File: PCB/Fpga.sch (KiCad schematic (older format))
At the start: 17 parts

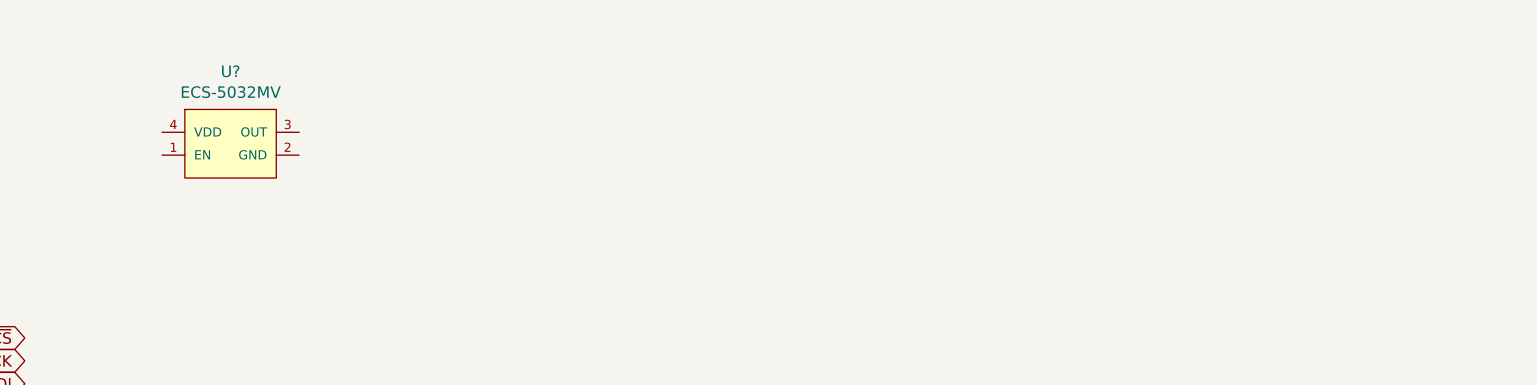
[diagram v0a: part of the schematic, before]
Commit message: Connect oscillator to power
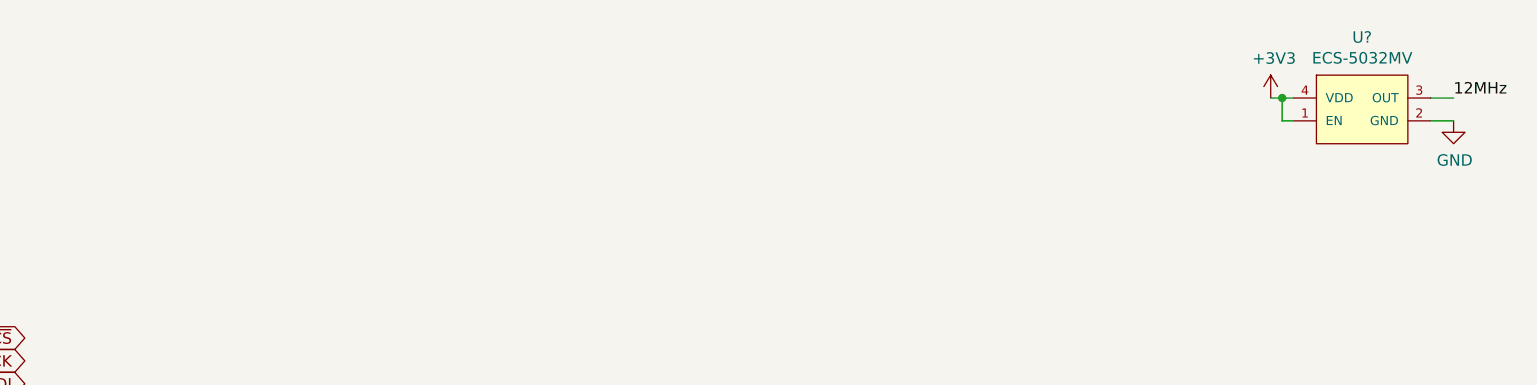
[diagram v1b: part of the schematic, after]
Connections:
- net +3V3: now also U?.1 (EN), U?.4 (VDD)
- net GND: now also U?.2 (GND)
- net 12MHz: now reaches U?.3 (OUT)
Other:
- moved on the sheet: U?
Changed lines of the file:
@@
 L Parts:ECS-5032MV U?
 U 1 1 5DD22CF7
-P 5450 1150
-F 0 "U?" H 5450 1465 50  0000 C CNN
-F 1 "ECS-5032MV" H 5450 1374 50  0000 C CNN
-F 2 "Parts:ECS-5032MV" H 5450 850 50  0001 C CNN
-F 3 "https://ecsxtal.com/ecs-5032mv" H 5450 750 50  0001 C CNN
-	1    5450 1150
+P 10400 1000
+F 0 "U?" H 10400 1315 50  0000 C CNN
+F 1 "ECS-5032MV" H 10400 1224 50  0000 C CNN
+F 2 "Parts:ECS-5032MV" H 10400 700 50  0001 C CNN
+F 3 "https://ecsxtal.com/ecs-5032mv" H 10400 600 50  0001 C CNN
+	1    10400 1000
 	1    0    0    -1
 $EndComp
@@
 Text GLabel 5750 5800 0    50   Input ~ 0
 FPGA-LINK4
+$Comp
+L power:+3V3 #PWR?
+U 1 1 5DD97BF5
+P 10000 950
+F 0 "#PWR?" H 10000 800 50  0001 C CNN
+F 1 "+3V3" H 10015 1123 50  0000 C CNN
+F 2 "" H 10000 950 50  0001 C CNN
+F 3 "" H 10000 950 50  0001 C CNN
+	1    10000 950
+	1    0    0    -1
+$EndComp
+Wire Wire Line
+	10000 950  10050 950
+$Comp
+L power:GND #PWR?
+U 1 1 5DD9CD01
+P 10800 1050
+F 0 "#PWR?" H 10800 800 50  0001 C CNN
+F 1 "GND" H 10805 877 50  0000 C CNN
+F 2 "" H 10800 1050 50  0001 C CNN
+F 3 "" H 10800 1050 50  0001 C CNN
+	1    10800 1050
+	1    0    0    -1
+$EndComp
+Wire Wire Line
+	10700 1050 10800 1050
+Text Label 10800 950  0    50   ~ 0
+12MHz
+Wire Wire Line
+	10700 950  10800 950
+Wire Wire Line
+	10050 950  10050 1050
+Wire Wire Line
+	10050 1050 10100 1050
+Connection ~ 10050 950
+Wire Wire Line
+	10050 950  10100 950
 $EndSCHEMATC

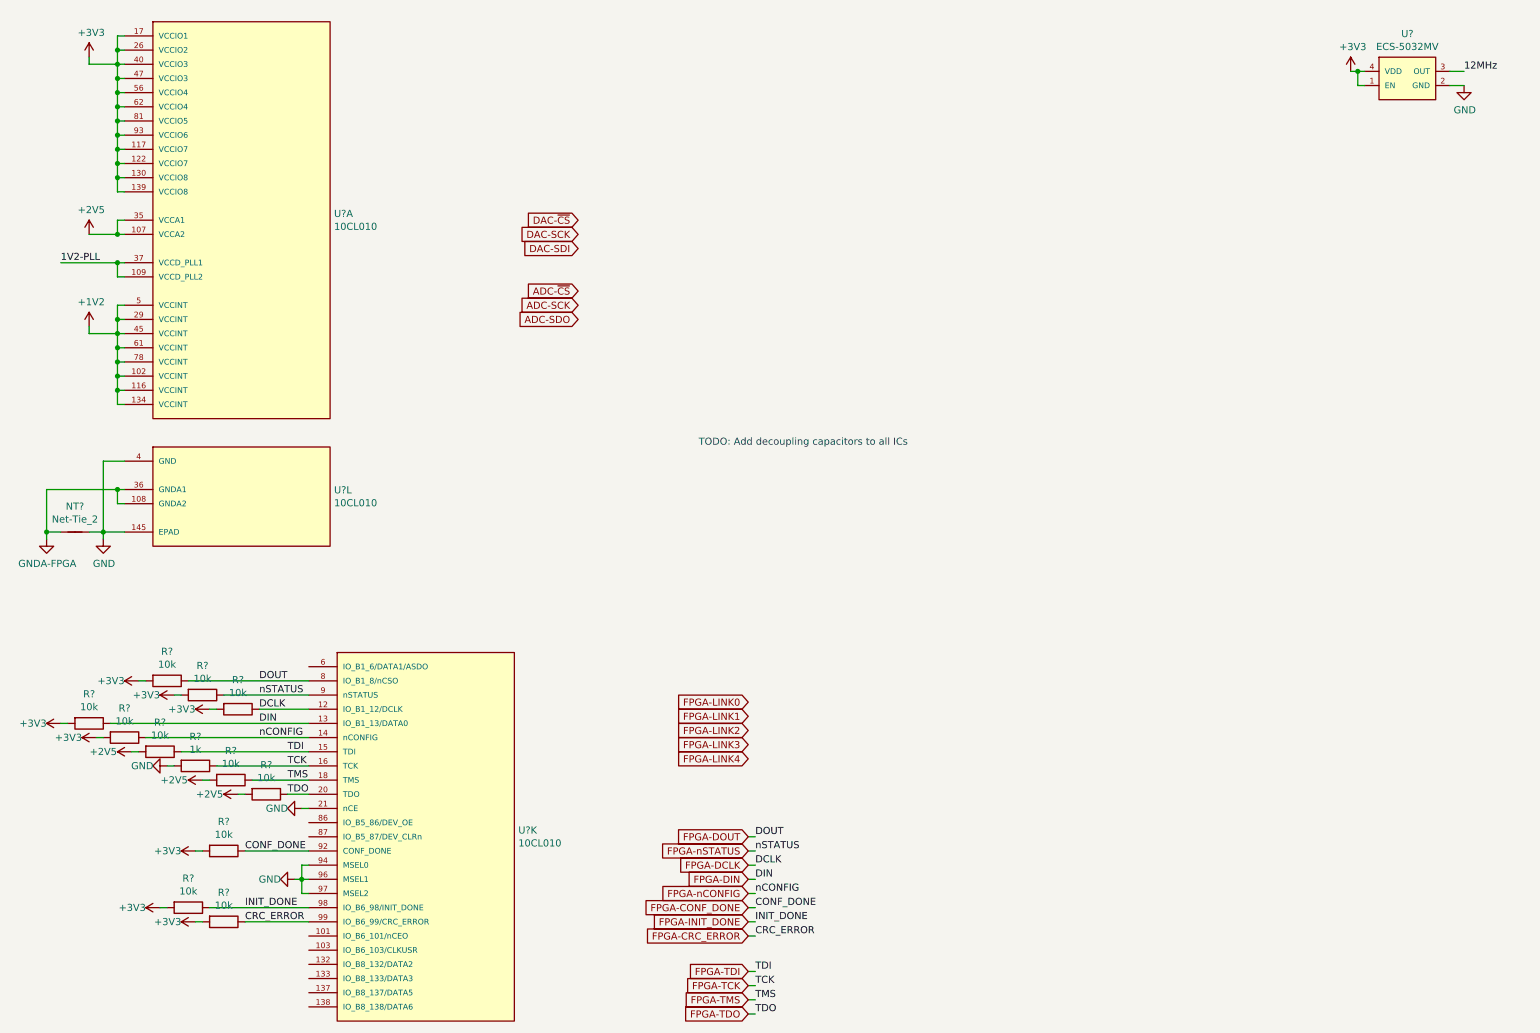
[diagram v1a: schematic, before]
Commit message: Added low-noise supply rails, changed 100nF capacitors to 0603 footprint, fixed ENS210 footprint, added decoupling capacitors to microcontroller
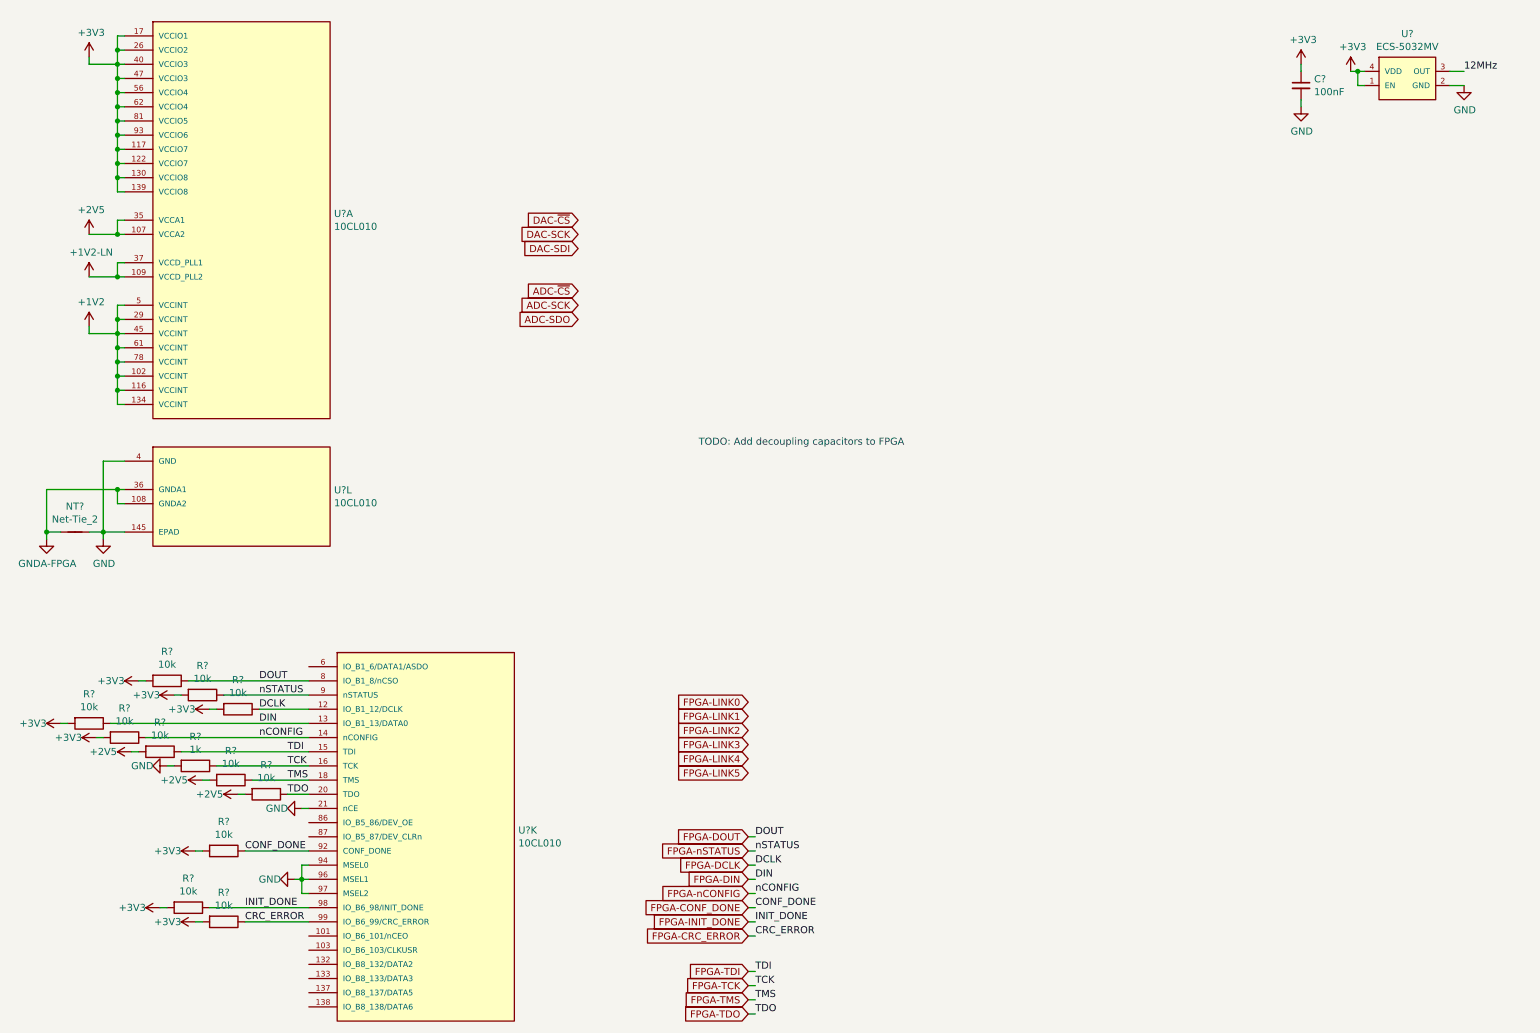
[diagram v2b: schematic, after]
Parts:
- added C?: 100nF, Capacitors_SMD:C_0603_HandSoldering, symbol Device:C_Small
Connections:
- net +3V3: now also C?.1
- net GND: now also C?.2
- net 1V2-PLL renamed +1V2-LN
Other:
- note added: "TODO: Add decoupling capacitors to FPGA"
- note removed: "TODO: Add decoupling capacitors to all ICs"
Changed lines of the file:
@@
 Wire Wire Line
 	1300 2400 1350 2400
-Text Label 900  2300 0    50   ~ 0
-1V2-PLL
 Wire Wire Line
 	1300 2300 1300 2400
-Wire Wire Line
-	900  2300 1300 2300
-Connection ~ 1300 2300
 Text GLabel 4550 2000 0    50   Input ~ 0
 DAC-~CS
@@
 	5750 6350 5800 6350
 Text Notes 5400 3600 0    50   ~ 0
-TODO: Add decoupling capacitors to all ICs
+TODO: Add decoupling capacitors to FPGA
 Text GLabel 5750 5400 0    50   Input ~ 0
 FPGA-LINK0
@@
 Wire Wire Line
 	10050 950  10100 950
+$Comp
+L Parts:+1V2-LN #PWR?
+U 1 1 5DD72B66
+P 1100 2400
+F 0 "#PWR?" H 1100 2250 50  0001 C CNN
+F 1 "+1V2-LN" H 1115 2573 50  0000 C CNN
+F 2 "" H 1100 2400 50  0001 C CNN
+F 3 "" H 1100 2400 50  0001 C CNN
+	1    1100 2400
+	1    0    0    -1
+$EndComp
+Wire Wire Line
+	1100 2400 1300 2400
+Connection ~ 1300 2400
+$Comp
+L Device:C_Small C?
+U 1 1 5DD852FA
+P 9650 1050
+F 0 "C?" H 9742 1096 50  0000 L CNN
+F 1 "100nF" H 9742 1005 50  0000 L CNN
+F 2 "Capacitors_SMD:C_0603_HandSoldering" H 9650 1050 50  0001 C CNN
+F 3 "https://www.digikey.ca/product-detail/en/w-rth-elektronik/885012206020/732-7939-1-ND/5454566" H 9650 1050 50  0001 C CNN
+	1    9650 1050
+	1    0    0    -1
+$EndComp
+$Comp
+L power:+3V3 #PWR?
+U 1 1 5DD89B39
+P 9650 900
+F 0 "#PWR?" H 9650 750 50  0001 C CNN
+F 1 "+3V3" H 9665 1073 50  0000 C CNN
+F 2 "" H 9650 900 50  0001 C CNN
+F 3 "" H 9650 900 50  0001 C CNN
+	1    9650 900
+	1    0    0    -1
+$EndComp
+Wire Wire Line
+	9650 900  9650 950
+$Comp
+L power:GND #PWR?
+U 1 1 5DD8DD81
+P 9650 1200
+F 0 "#PWR?" H 9650 950 50  0001 C CNN
+F 1 "GND" H 9655 1027 50  0000 C CNN
+F 2 "" H 9650 1200 50  0001 C CNN
+F 3 "" H 9650 1200 50  0001 C CNN
+	1    9650 1200
+	1    0    0    -1
+$EndComp
+Wire Wire Line
+	9650 1150 9650 1200
+Text GLabel 5750 5900 0    50   Input ~ 0
+FPGA-LINK5
 $EndSCHEMATC

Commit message: Add decoupling and bulk capacitance for FPGA
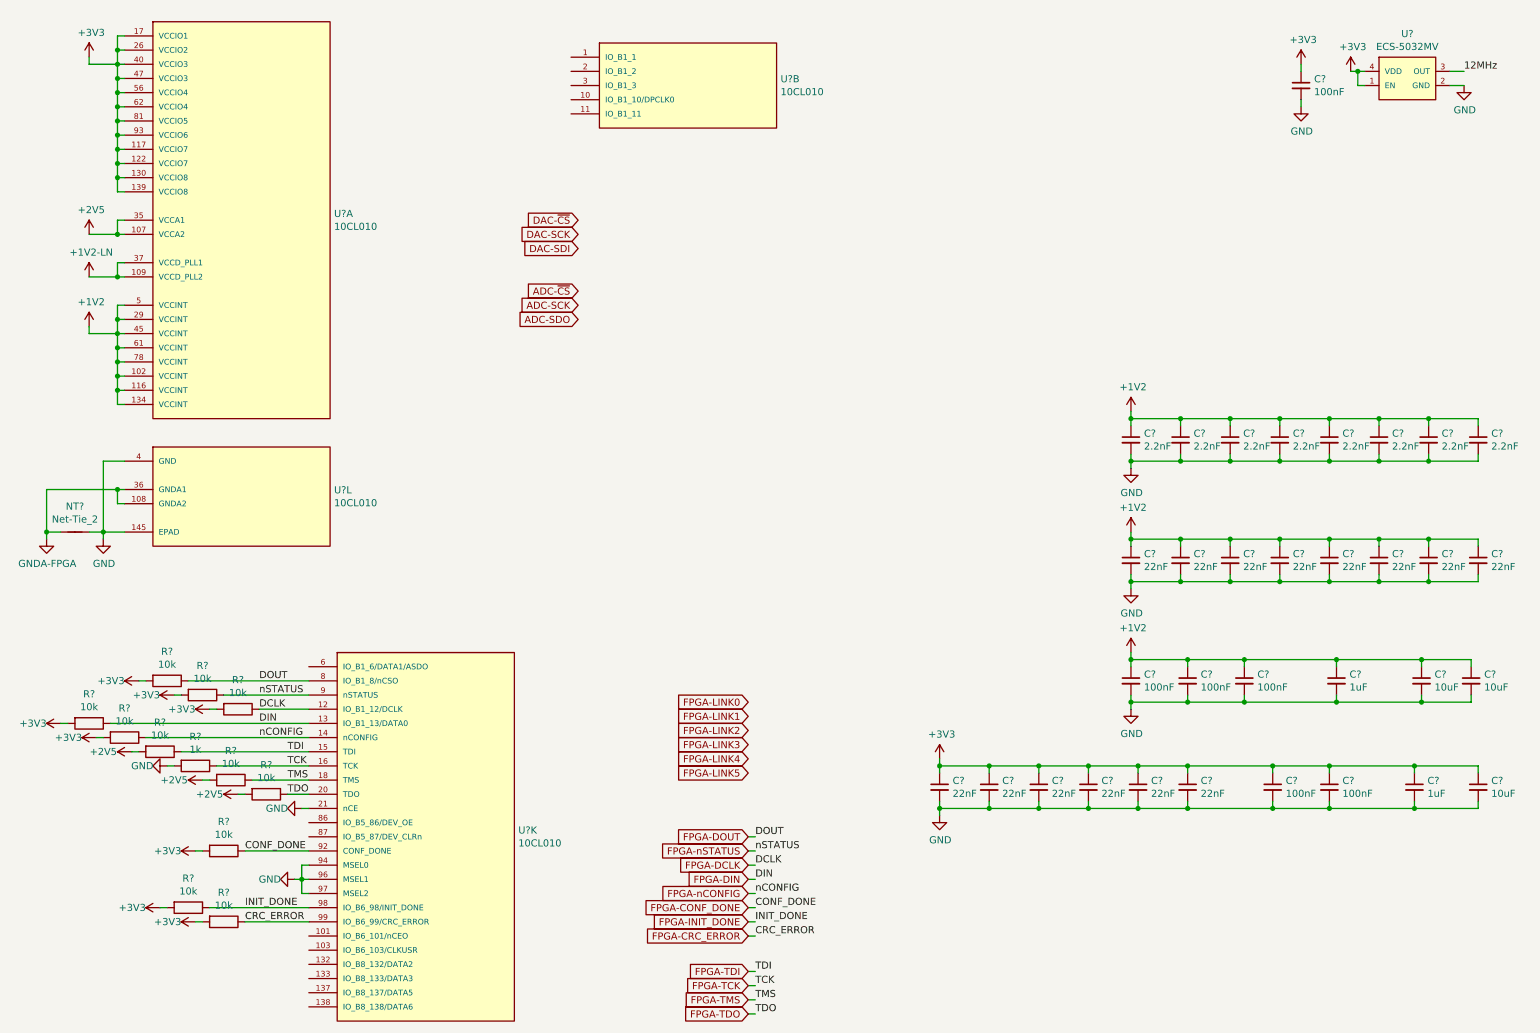
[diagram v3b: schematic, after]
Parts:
- added C? (x5): 100nF, Capacitors_SMD:C_0603_HandSoldering, symbol Device:C_Small
- added C? (x2): 1uF, Capacitors_SMD:C_0603_HandSoldering, symbol Device:C_Small
- added C? (x3): 10uF, Capacitors_SMD:C_0805_HandSoldering, symbol Device:C_Small
- added C? (x14): 22nF, Capacitors_SMD:C_0603_HandSoldering, symbol Device:C_Small
- added C? (x8): 2.2nF, Capacitors_SMD:C_0603_HandSoldering, symbol Device:C_Small
- added U?: 10CL010, Parts:EQFP144-PAD, symbol Parts:10CL010
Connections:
- net +1V2: now also C?.1, C?.1, C?.1, C?.1, C?.1, C?.1, C?.1, C?.1, C?.1, C?.1, C?.1, C?.1, C?.1, C?.1, C?.1, C?.1, C?.1, C?.1, C?.1, C?.1, C?.1, C?.1
- net +3V3: now also C?.1, C?.1, C?.1, C?.1, C?.1, C?.1, C?.1, C?.1, C?.1, C?.1
- net GND: now also C?.2, C?.2, C?.2, C?.2, C?.2, C?.2, C?.2, C?.2, C?.2, C?.2, C?.2, C?.2, C?.2, C?.2, C?.2, C?.2, C?.2, C?.2, C?.2, C?.2, C?.2, C?.2, C?.2, C?.2, C?.2, C?.2, C?.2, C?.2, C?.2, C?.2, C?.2, C?.2
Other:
- note removed: "TODO: Add decoupling capacitors to FPGA"

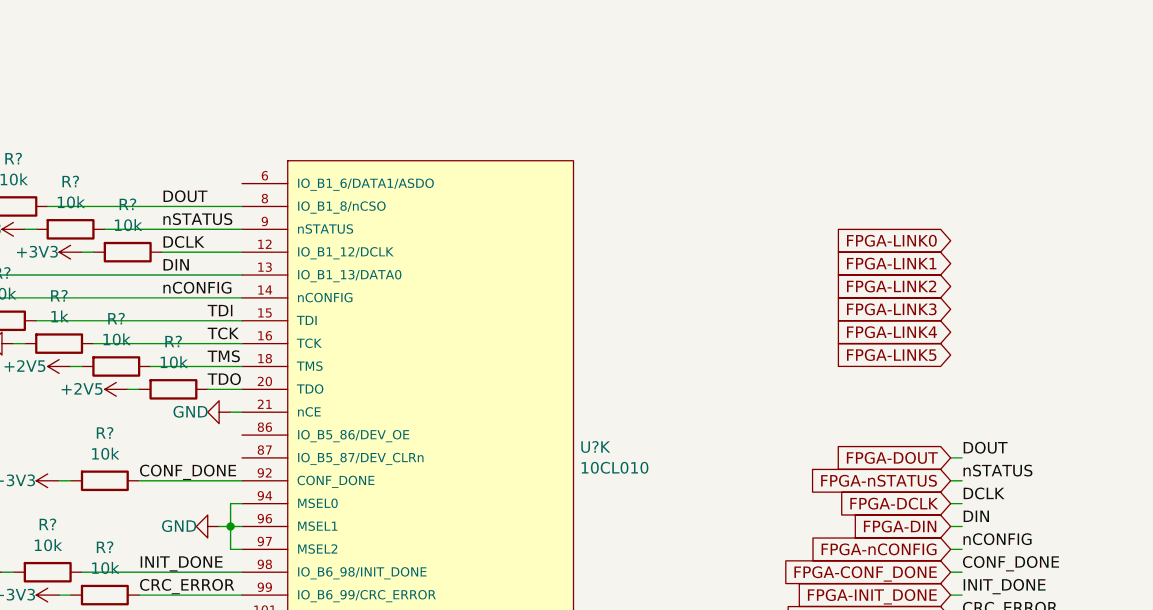
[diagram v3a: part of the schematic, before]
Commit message: Add comparator to monitor 50V supply, add flash memory for storing FPGA config data
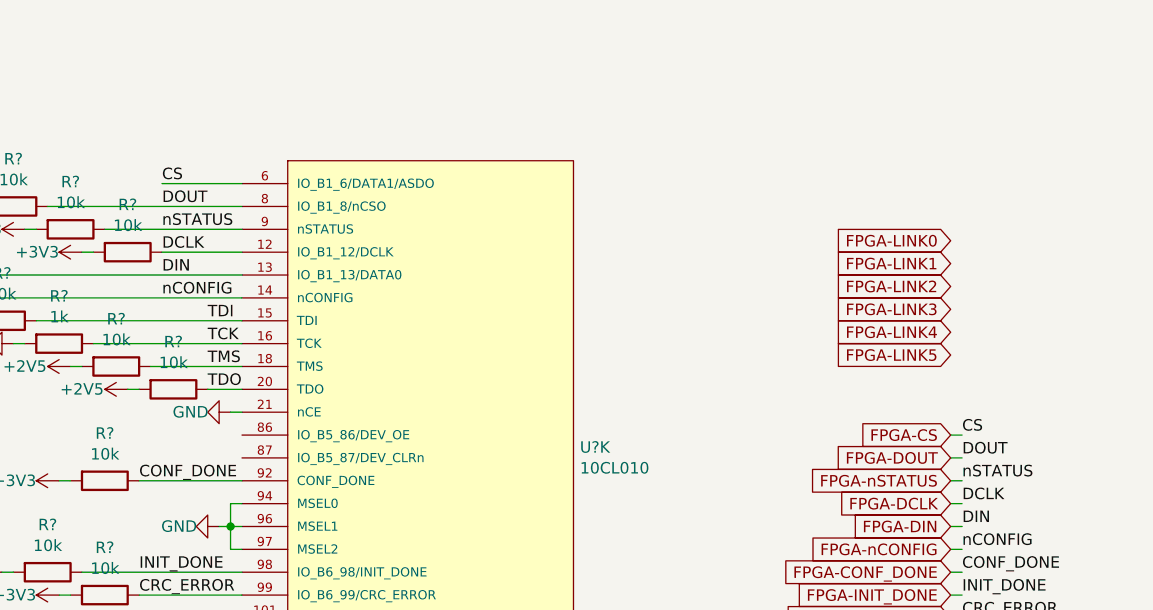
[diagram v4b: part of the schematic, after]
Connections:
- net FPGA-CS: now reaches U?.6 (IO_B1_6/DATA1/ASDO)
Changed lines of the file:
@@
 	1    0    0    -1
 $EndComp
+Text GLabel 5750 6250 0    50   Input ~ 0
+FPGA-CS
+Text Label 2300 5150 0    50   ~ 0
+CS
+Wire Wire Line
+	2300 5150 2650 5150
+Text Label 5800 6250 0    50   ~ 0
+CS
+Wire Wire Line
+	5750 6250 5800 6250
 $EndSCHEMATC
